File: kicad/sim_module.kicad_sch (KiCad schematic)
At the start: 2 parts, among them J40 693043020611, U40 TPD3F303DPVR

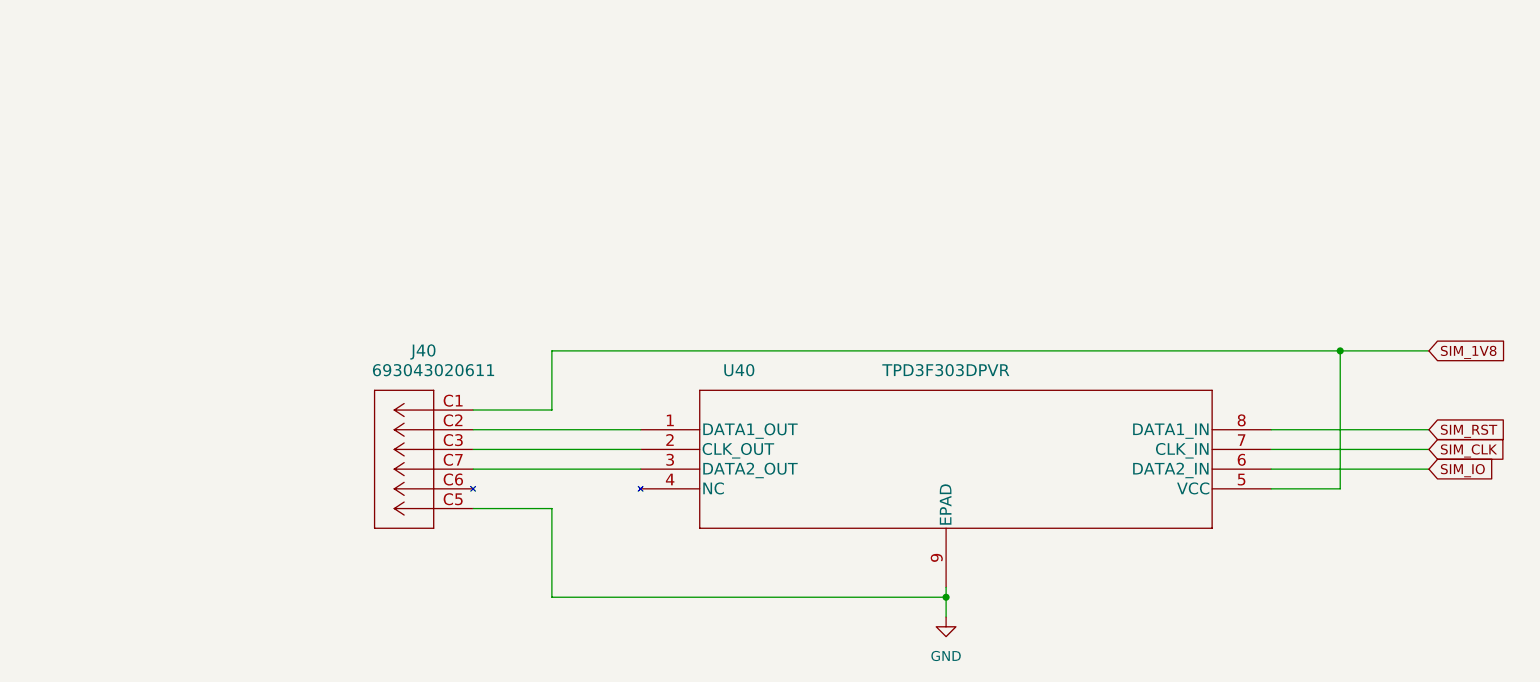
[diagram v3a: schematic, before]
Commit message: Added Digikey part number and footprint to symbols, added signal TMP_ALERT
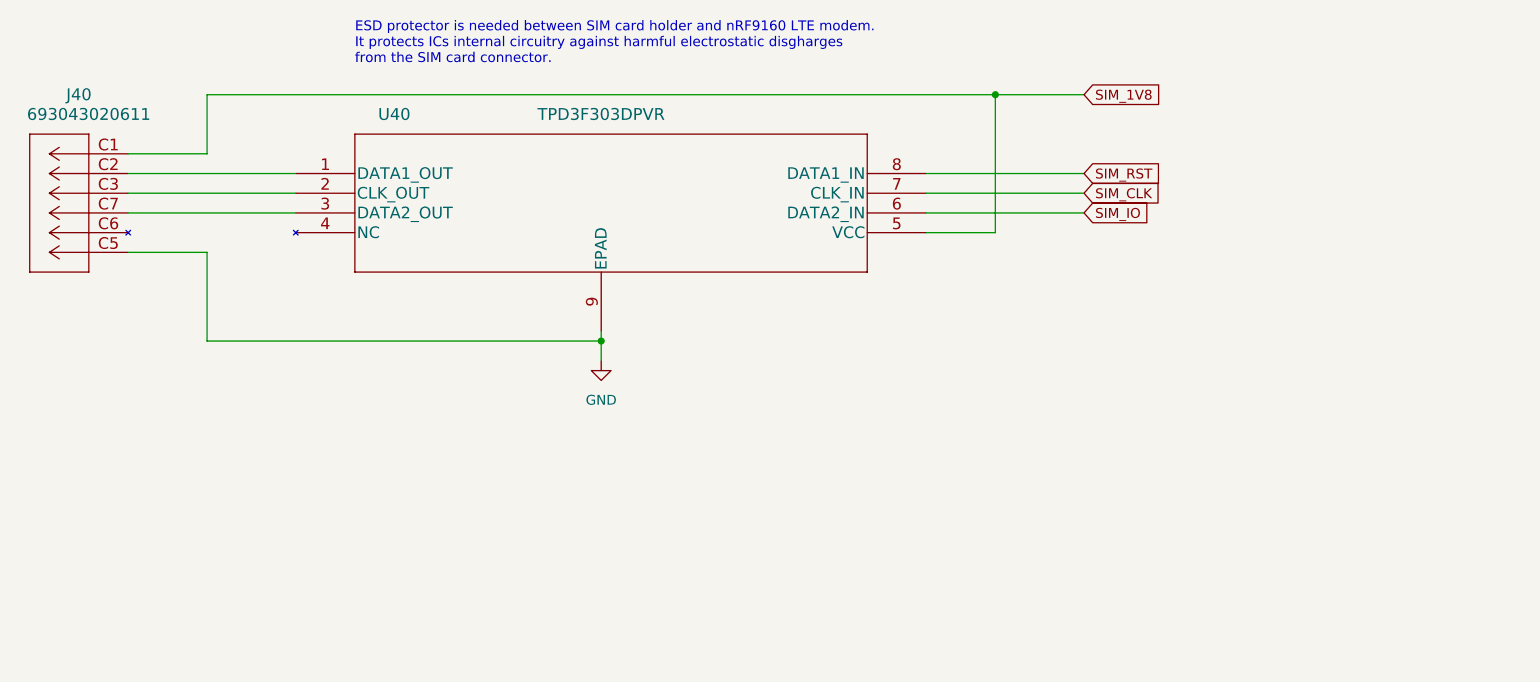
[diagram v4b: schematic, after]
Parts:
- J40: footprint CONN6_43020611_WRE -> 693043020611:693043020611; Digikey (none) -> 296-28299-1-ND
- U40: footprint DPV8_1P7X0P4 -> TPD3F303DPVR:TPD3F303DPVR; Digikey (none) -> 732-5954-1-ND
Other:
- note added: "ESD protector is needed between SIM card holder and nRF9160 LTE modem. It protects ICs internal circuitry against harmful electrostatic disgharges from the SIM card connector."
- moved on the sheet: J40, U40
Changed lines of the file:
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@@
 (kicad_sch (version 20230121) (generator eeschema)
-  (paper "A4")
+  (paper "A5")
   (title_block
     (title "SIM module")
@@
     (comment 1 "SIM card holder and ESD protector")
   )
-  (junction (at 201.93 74.93) (diameter 0) (color 0 0 0 0)
+  (junction (at 157.48 41.91) (diameter 0) (color 0 0 0 0)
   )
-  (junction (at 151.13 106.68) (diameter 0) (color 0 0 0 0)
+  (junction (at 106.68 73.66) (diameter 0) (color 0 0 0 0)
   )
-  (wire (pts (xy 100.33 95.25) (xy 100.33 106.68))
+  (wire (pts (xy 55.88 62.23) (xy 55.88 73.66))
     (stroke (width 0) (type default))
   )
-  (wire (pts (xy 201.93 74.93) (xy 213.36 74.93))
+  (wire (pts (xy 157.48 41.91) (xy 168.91 41.91))
     (stroke (width 0) (type default))
   )
-  (wire (pts (xy 90.17 82.55) (xy 100.33 82.55))
+  (wire (pts (xy 45.72 49.53) (xy 55.88 49.53))
     (stroke (width 0) (type default))
   )
-  (wire (pts (xy 193.04 87.63) (xy 213.36 87.63))
+  (wire (pts (xy 148.59 54.61) (xy 168.91 54.61))
     (stroke (width 0) (type default))
   )
-  (wire (pts (xy 100.33 74.93) (xy 201.93 74.93))
+  (wire (pts (xy 55.88 41.91) (xy 157.48 41.91))
     (stroke (width 0) (type default))
   )
-  (wire (pts (xy 90.17 85.09) (xy 111.76 85.09))
+  (wire (pts (xy 45.72 52.07) (xy 67.31 52.07))
     (stroke (width 0) (type default))
   )
-  (wire (pts (xy 193.04 92.71) (xy 201.93 92.71))
+  (wire (pts (xy 148.59 59.69) (xy 157.48 59.69))
     (stroke (width 0) (type default))
   )
-  (wire (pts (xy 193.04 85.09) (xy 213.36 85.09))
+  (wire (pts (xy 148.59 52.07) (xy 168.91 52.07))
     (stroke (width 0) (type default))
   )
-  (wire (pts (xy 100.33 82.55) (xy 100.33 74.93))
+  (wire (pts (xy 55.88 49.53) (xy 55.88 41.91))
     (stroke (width 0) (type default))
   )
-  (wire (pts (xy 90.17 90.17) (xy 111.76 90.17))
+  (wire (pts (xy 45.72 57.15) (xy 67.31 57.15))
     (stroke (width 0) (type default))
   )
-  (wire (pts (xy 151.13 105.41) (xy 151.13 106.68))
+  (wire (pts (xy 106.68 72.39) (xy 106.68 73.66))
     (stroke (width 0) (type default))
   )
-  (wire (pts (xy 151.13 106.68) (xy 151.13 109.22))
+  (wire (pts (xy 106.68 73.66) (xy 106.68 76.2))
     (stroke (width 0) (type default))
   )
-  (wire (pts (xy 90.17 95.25) (xy 100.33 95.25))
+  (wire (pts (xy 45.72 62.23) (xy 55.88 62.23))
     (stroke (width 0) (type default))
   )
-  (wire (pts (xy 90.17 87.63) (xy 111.76 87.63))
+  (wire (pts (xy 45.72 54.61) (xy 67.31 54.61))
     (stroke (width 0) (type default))
   )
-  (wire (pts (xy 193.04 90.17) (xy 213.36 90.17))
+  (wire (pts (xy 148.59 57.15) (xy 168.91 57.15))
     (stroke (width 0) (type default))
   )
-  (wire (pts (xy 201.93 74.93) (xy 201.93 92.71))
+  (wire (pts (xy 157.48 41.91) (xy 157.48 59.69))
     (stroke (width 0) (type default))
   )
-  (wire (pts (xy 100.33 106.68) (xy 151.13 106.68))
+  (wire (pts (xy 55.88 73.66) (xy 106.68 73.66))
     (stroke (width 0) (type default))
   )
-  (global_label "SIM_1V8" (shape input) (at 213.36 74.93 0) (fields_autoplaced)
+  (text "ESD protector is needed between SIM card holder and nRF9160 LTE modem.\nIt protects ICs internal circuitry against harmful electrostatic disgharges\nfrom the SIM card connector."
+    (at 74.93 38.1 0)
+    (effects (font (size 1.27 1.27)) (justify left bottom))
+  )
+  (global_label "SIM_1V8" (shape input) (at 168.91 41.91 0) (fields_autoplaced)
     (effects (font (size 1.27 1.27)) (justify left))
-    (property "Intersheetrefs" "${INTERSHEET_REFS}" (at 224.0067 74.93 0)
+    (property "Intersheetrefs" "${INTERSHEET_REFS}" (at 179.5567 41.91 0)
       (effects (font (size 1.27 1.27)) (justify left) hide)
     )
   )
-  (global_label "SIM_IO" (shape input) (at 213.36 90.17 0) (fields_autoplaced)
+  (global_label "SIM_IO" (shape input) (at 168.91 57.15 0) (fields_autoplaced)
     (effects (font (size 1.27 1.27)) (justify left))
-    (property "Intersheetrefs" "${INTERSHEET_REFS}" (at 222.4344 90.17 0)
+    (property "Intersheetrefs" "${INTERSHEET_REFS}" (at 177.9844 57.15 0)
       (effects (font (size 1.27 1.27)) (justify left) hide)
     )
   )
-  (global_label "SIM_CLK" (shape input) (at 213.36 87.63 0) (fields_autoplaced)
+  (global_label "SIM_CLK" (shape input) (at 168.91 54.61 0) (fields_autoplaced)
     (effects (font (size 1.27 1.27)) (justify left))
-    (property "Intersheetrefs" "${INTERSHEET_REFS}" (at 224.0672 87.63 0)
+    (property "Intersheetrefs" "${INTERSHEET_REFS}" (at 179.6172 54.61 0)
       (effects (font (size 1.27 1.27)) (justify left) hide)
     )
   )
-  (global_label "SIM_RST" (shape input) (at 213.36 85.09 0) (fields_autoplaced)
+  (global_label "SIM_RST" (shape input) (at 168.91 52.07 0) (fields_autoplaced)
     (effects (font (size 1.27 1.27)) (justify left))
-    (property "Intersheetrefs" "${INTERSHEET_REFS}" (at 223.9462 85.09 0)
+    (property "Intersheetrefs" "${INTERSHEET_REFS}" (at 179.4962 52.07 0)
       (effects (font (size 1.27 1.27)) (justify left) hide)
     )
   )
-  (symbol (lib_id "693043020611:693043020611") (at 90.17 82.55 0) (mirror y) (unit 1)
+  (symbol (lib_id "693043020611:693043020611") (at 45.72 49.53 0) (mirror y) (unit 1)
     (in_bom yes) (on_board yes) (dnp no)
-    (property "Reference" "J40" (at 83.82 74.93 0)
+    (property "Reference" "J40" (at 39.37 41.91 0)
       (effects (font (size 1.524 1.524)))
     )
-    (property "Value" "693043020611" (at 85.09 77.47 0)
+    (property "Value" "693043020611" (at 40.64 44.45 0)
       (effects (font (size 1.524 1.524)))
     )
-    (property "Footprint" "CONN6_43020611_WRE" (at 80.01 75.946 0)
+    (property "Footprint" "693043020611:693043020611" (at 35.56 42.926 0)
       (effects (font (size 1.524 1.524)) hide)
     )
-    (property "Datasheet" "" (at 90.17 82.55 0)
+    (property "Datasheet" "" (at 45.72 49.53 0)
       (effects (font (size 1.524 1.524)))
+    )
+    (property "Digikey" "296-28299-1-ND" (at 45.72 49.53 0)
+      (effects (font (size 1.27 1.27)) hide)
     )
     (pin "C1")
@@
     )
   )
-  (symbol (lib_id "TPD3F303DPVR:TPD3F303DPVR") (at 111.76 85.09 0) (unit 1)
+  (symbol (lib_id "TPD3F303DPVR:TPD3F303DPVR") (at 67.31 52.07 0) (unit 1)
     (in_bom yes) (on_board yes) (dnp no)
-    (property "Reference" "U40" (at 124.46 77.47 0)
+    (property "Reference" "U40" (at 80.01 44.45 0)
       (effects (font (size 1.524 1.524)))
     )
-    (property "Value" "TPD3F303DPVR" (at 151.13 77.47 0)
+    (property "Value" "TPD3F303DPVR" (at 106.68 44.45 0)
       (effects (font (size 1.524 1.524)))
     )
-    (property "Footprint" "DPV8_1P7X0P4" (at 71.12 91.186 0)
+    (property "Footprint" "TPD3F303DPVR:TPD3F303DPVR" (at 26.67 58.166 0)
       (effects (font (size 1.524 1.524)) hide)
     )
-    (property "Datasheet" "" (at 111.76 85.09 0)
+    (property "Datasheet" "" (at 67.31 52.07 0)
       (effects (font (size 1.524 1.524)))
+    )
+    (property "Digikey" "732-5954-1-ND" (at 67.31 52.07 0)
+      (effects (font (size 1.27 1.27)) hide)
     )
     (pin "1")
@@
     )
   )
-  (symbol (lib_id "power:GND") (at 151.13 109.22 0) (unit 1)
+  (symbol (lib_id "power:GND") (at 106.68 76.2 0) (unit 1)
     (in_bom yes) (on_board yes) (dnp no) (fields_autoplaced)
-    (property "Reference" "#PWR03" (at 151.13 115.57 0)
+    (property "Reference" "#PWR03" (at 106.68 82.55 0)
       (effects (font (size 1.27 1.27)) hide)
     )
-    (property "Value" "GND" (at 151.13 114.3 0)
+    (property "Value" "GND" (at 106.68 81.28 0)
       (effects (font (size 1.27 1.27)))
     )
-    (property "Footprint" "" (at 151.13 109.22 0)
+    (property "Footprint" "" (at 106.68 76.2 0)
       (effects (font (size 1.27 1.27)) hide)
     )
-    (property "Datasheet" "" (at 151.13 109.22 0)
+    (property "Datasheet" "" (at 106.68 76.2 0)
       (effects (font (size 1.27 1.27)) hide)
     )

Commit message: ESD change
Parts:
- removed U40: TPD3F303DPVR, TPD3F303DPVR:TPD3F303DPVR, symbol TPD3F303DPVR:TPD3F303DPVR
- added U1: TPD3F303DQDR, TPD3F303DQDR:TPD3F303DQDR, symbol TPD3F303DQDR:TPD3F303DQDR
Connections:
- net GND: now also U1.9 (EPAD)
- net SIM_1V8: now also U1.5 (VCC)
- net SIM_CLK: now also U1.7 (CLK_IN)
- net SIM_IO: now also U1.6 (DATA2_IN)
- net SIM_RST: now also U1.8 (DATA1_IN)
- net at J40.C2: now also U1.1 (DATA1_OUT)
- net at J40.C3: now also U1.2 (CLK_OUT)
- net at J40.C7: now also U1.3 (DATA2_OUT)
- no-connect marks 0 -> 1
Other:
- moved on the sheet: J40
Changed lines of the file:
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@@
   (junction (at 106.68 73.66) (diameter 0) (color 0 0 0 0)
   )
-  (wire (pts (xy 55.88 62.23) (xy 55.88 73.66))
+  (no_connect (at 67.31 57.15))
+  (wire (pts (xy 45.72 49.53) (xy 67.31 49.53))
+    (stroke (width 0) (type default))
+  )
+  (wire (pts (xy 55.88 59.69) (xy 55.88 73.66))
     (stroke (width 0) (type default))
   )
@@
     (stroke (width 0) (type default))
   )
-  (wire (pts (xy 45.72 49.53) (xy 55.88 49.53))
+  (wire (pts (xy 45.72 46.99) (xy 55.88 46.99))
+    (stroke (width 0) (type default))
+  )
+  (wire (pts (xy 148.59 49.53) (xy 151.13 49.53))
     (stroke (width 0) (type default))
   )
@@
     (stroke (width 0) (type default))
   )
+  (wire (pts (xy 45.72 52.07) (xy 67.31 52.07))
+    (stroke (width 0) (type default))
+  )
   (wire (pts (xy 55.88 41.91) (xy 157.48 41.91))
     (stroke (width 0) (type default))
   )
-  (wire (pts (xy 45.72 52.07) (xy 67.31 52.07))
+  (wire (pts (xy 151.13 73.66) (xy 106.68 73.66))
     (stroke (width 0) (type default))
   )
@@
     (stroke (width 0) (type default))
   )
-  (wire (pts (xy 55.88 49.53) (xy 55.88 41.91))
+  (wire (pts (xy 55.88 59.69) (xy 45.72 59.69))
     (stroke (width 0) (type default))
   )
-  (wire (pts (xy 45.72 57.15) (xy 67.31 57.15))
+  (wire (pts (xy 55.88 41.91) (xy 55.88 46.99))
     (stroke (width 0) (type default))
   )
-  (wire (pts (xy 106.68 72.39) (xy 106.68 73.66))
+  (wire (pts (xy 151.13 49.53) (xy 151.13 73.66))
     (stroke (width 0) (type default))
   )
   (wire (pts (xy 106.68 73.66) (xy 106.68 76.2))
-    (stroke (width 0) (type default))
-  )
-  (wire (pts (xy 45.72 62.23) (xy 55.88 62.23))
     (stroke (width 0) (type default))
   )
@@
     )
   )
-  (symbol (lib_id "693043020611:693043020611") (at 45.72 49.53 0) (mirror y) (unit 1)
+  (symbol (lib_id "693043020611:693043020611") (at 45.72 46.99 0) (mirror y) (unit 1)
     (in_bom yes) (on_board yes) (dnp no)
-    (property "Reference" "J40" (at 39.37 41.91 0)
+    (property "Reference" "J40" (at 39.37 39.37 0)
       (effects (font (size 1.524 1.524)))
     )
-    (property "Value" "693043020611" (at 40.64 44.45 0)
+    (property "Value" "693043020611" (at 40.64 41.91 0)
       (effects (font (size 1.524 1.524)))
     )
-    (property "Footprint" "693043020611:693043020611" (at 35.56 42.926 0)
+    (property "Footprint" "693043020611:693043020611" (at 35.56 40.386 0)
       (effects (font (size 1.524 1.524)) hide)
     )
-    (property "Datasheet" "" (at 45.72 49.53 0)
+    (property "Datasheet" "" (at 45.72 46.99 0)
       (effects (font (size 1.524 1.524)))
     )
-    (property "Digikey" "296-28299-1-ND" (at 45.72 49.53 0)
+    (property "Digikey" "296-28299-1-ND" (at 45.72 46.99 0)
       (effects (font (size 1.27 1.27)) hide)
     )
@@
         (path "/184b47ed-2c2b-4c02-be35-d18f4f4e5685/38627e9e-7096-4a1a-bc9e-0f2735fcbe8c"
           (reference "J40") (unit 1)
-        )
-      )
-    )
-  )
-  (symbol (lib_id "TPD3F303DPVR:TPD3F303DPVR") (at 67.31 52.07 0) (unit 1)
-    (in_bom yes) (on_board yes) (dnp no)
-    (property "Reference" "U40" (at 80.01 44.45 0)
-      (effects (font (size 1.524 1.524)))
-    )
-    (property "Value" "TPD3F303DPVR" (at 106.68 44.45 0)
-      (effects (font (size 1.524 1.524)))
-    )
-    (property "Footprint" "TPD3F303DPVR:TPD3F303DPVR" (at 26.67 58.166 0)
-      (effects (font (size 1.524 1.524)) hide)
-    )
-    (property "Datasheet" "" (at 67.31 52.07 0)
-      (effects (font (size 1.524 1.524)))
-    )
-    (property "Digikey" "732-5954-1-ND" (at 67.31 52.07 0)
-      (effects (font (size 1.27 1.27)) hide)
-    )
-    (pin "1")
-    (pin "2")
-    (pin "3")
-    (pin "4")
-    (pin "5")
-    (pin "6")
-    (pin "7")
-    (pin "8")
-    (pin "9")
-    (instances
-      (project "IoT_sulari"
-        (path "/184b47ed-2c2b-4c02-be35-d18f4f4e5685/38627e9e-7096-4a1a-bc9e-0f2735fcbe8c"
-          (reference "U40") (unit 1)
         )
       )
@@
         )
       )
+    )
+  )
+  (symbol (lib_id "TPD3F303DQDR:TPD3F303DQDR") (at 67.31 49.53 0) (unit 1)
+    (in_bom yes) (on_board yes) (dnp no) (fields_autoplaced)
+    (property "Reference" "U1" (at 107.95 40.64 0)
+      (effects (font (size 1.524 1.524)))
+    )
+    (property "Value" "TPD3F303DQDR" (at 107.95 43.18 0)
+      (effects (font (size 1.524 1.524)))
+    )
+    (property "Footprint" "TPD3F303DQDR:TPD3F303DQDR" (at 67.31 49.53 0)
+      (effects (font (size 1.27 1.27) italic) hide)
+    )
+    (property "Datasheet" "TPD3F303DQDR" (at 67.31 49.53 0)
+      (effects (font (size 1.27 1.27) italic) hide)
+    )
+    (pin "1")
+    (pin "2")
+    (pin "3")
+    (pin "4")
+    (pin "5")
+    (pin "6")
+    (pin "7")
+    (pin "8")
+    (pin "9")
+    (instances
+      (project "IoT_sulari"
+        (path "/184b47ed-2c2b-4c02-be35-d18f4f4e5685/38627e9e-7096-4a1a-bc9e-0f2735fcbe8c"
+          (reference "U1") (unit 1)
+        )
+      )
